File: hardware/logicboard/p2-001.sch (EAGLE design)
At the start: 33 parts, among them IC1 5V, IC2 74LS07N, IC3 4066N, IC4 LTC485N, K1 G5V1, T1 2SC1815, U1 DS18B20

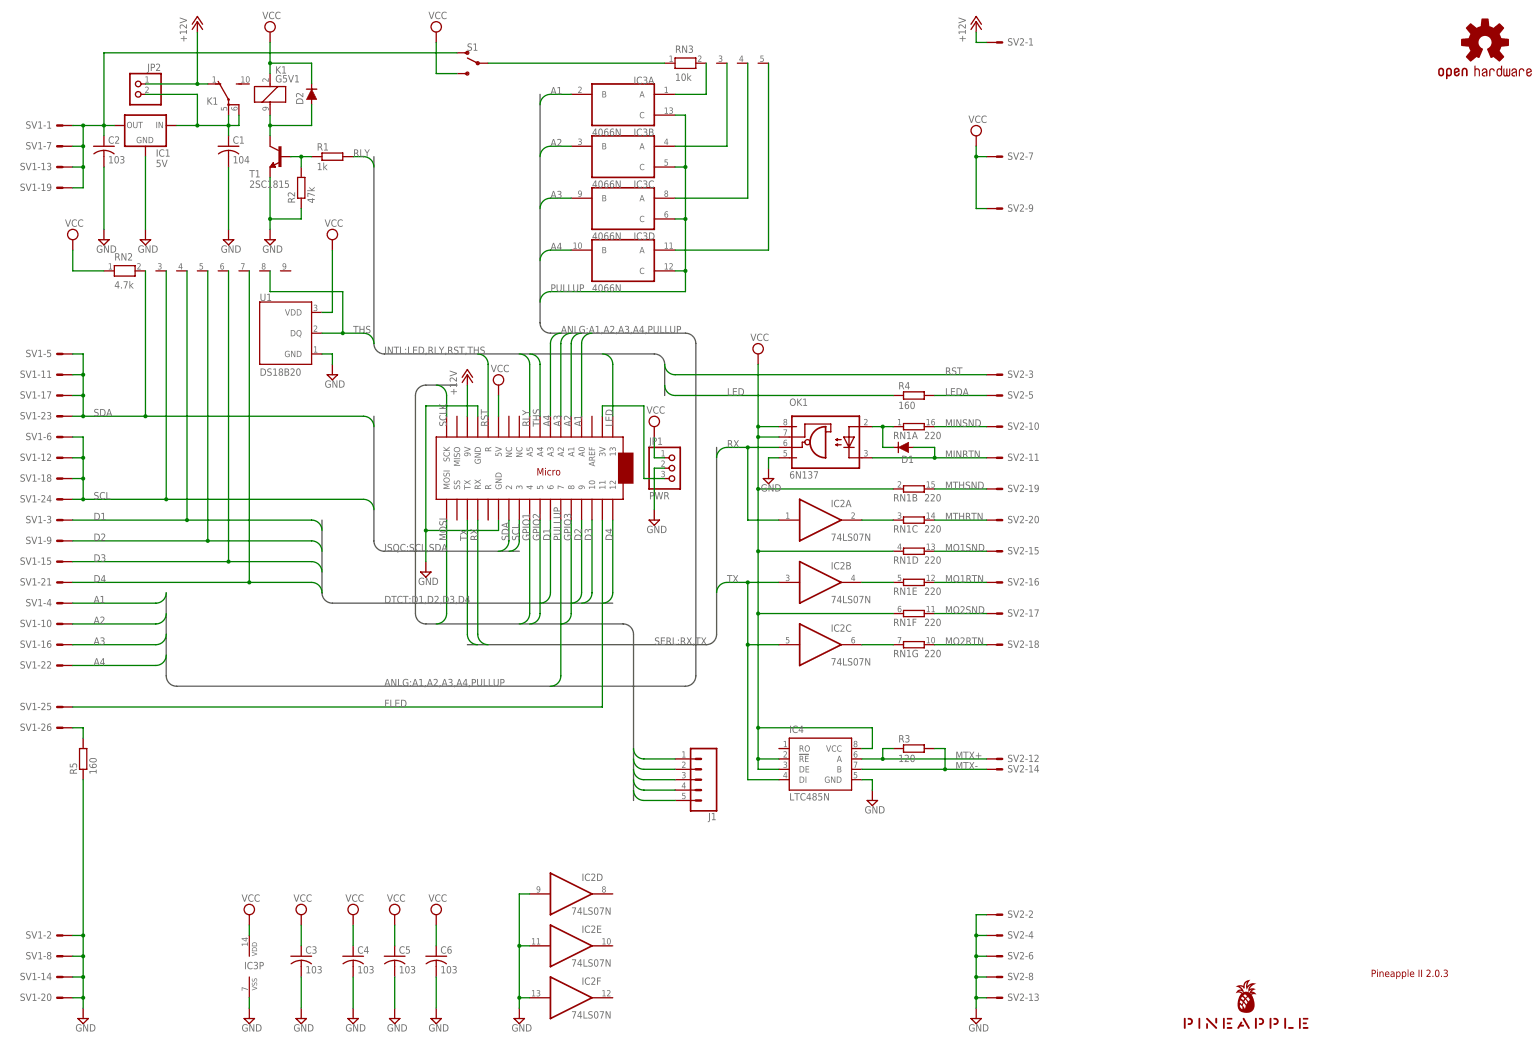
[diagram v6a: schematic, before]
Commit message: Renumbered parts.
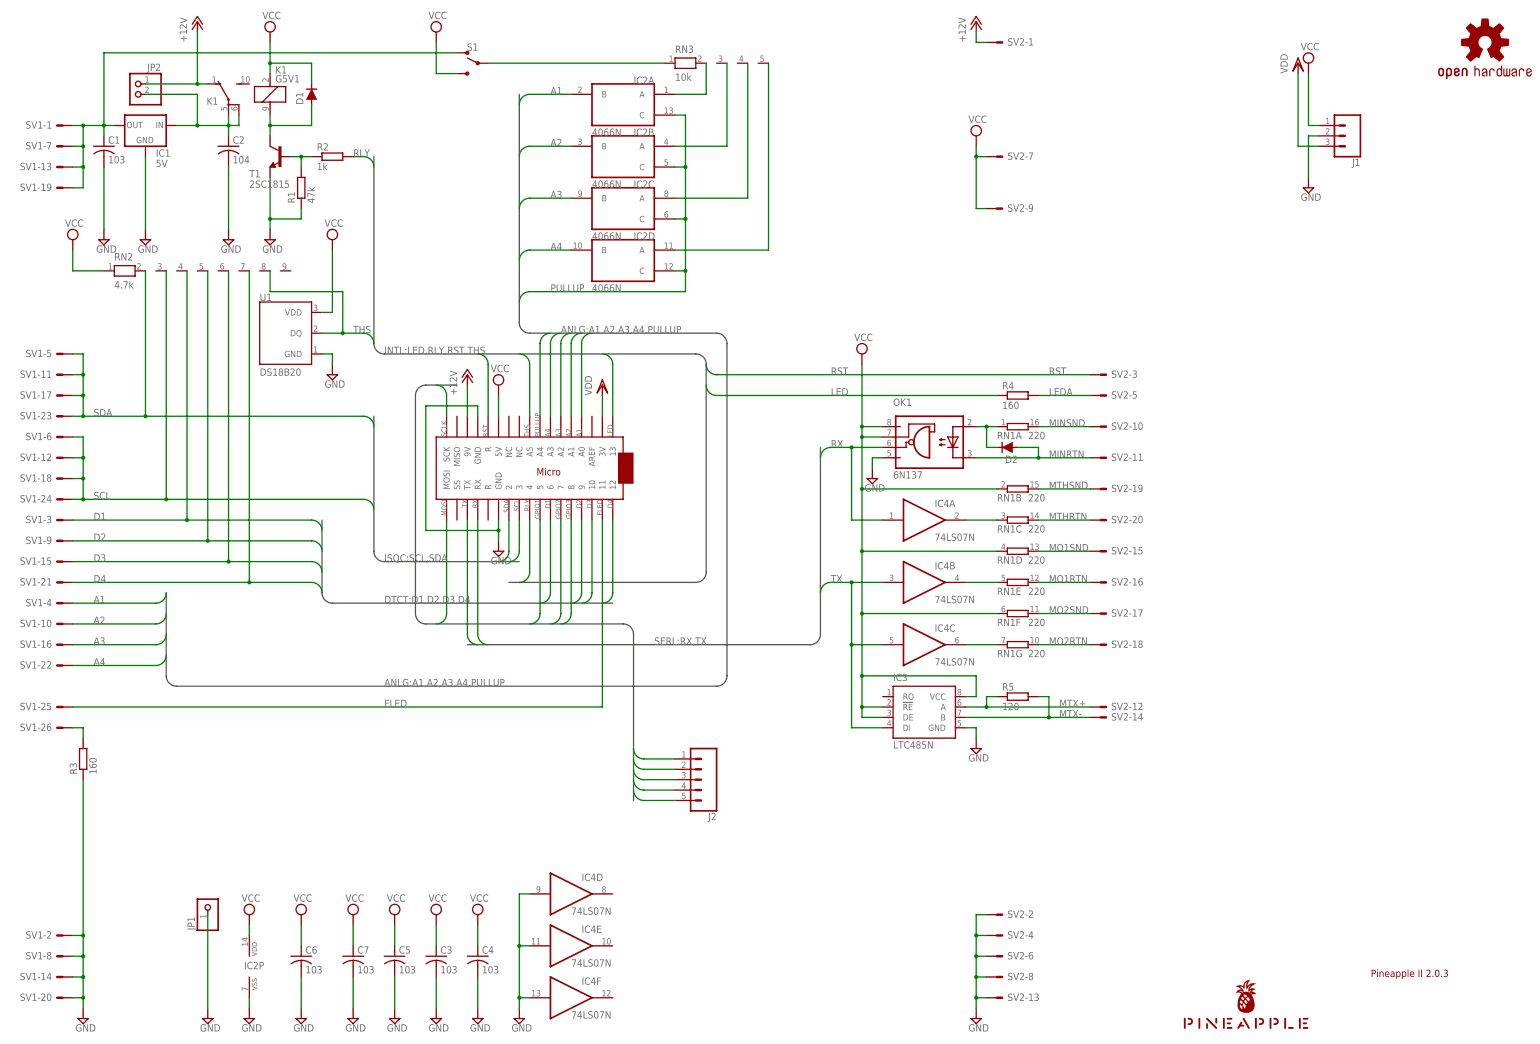
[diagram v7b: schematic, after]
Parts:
- added C7: 103, rcl:C-US025-025X050
- added J2: (no value), SparkFun-Connectors:CONN_05JST
- C1: value 104 -> 103
- C2: value 103 -> 104
- IC2: value 74LS07N -> 4066N; device 74xx-us:74LS07N -> 40xx:4066N
- IC3: value 4066N -> LTC485N; device 40xx:4066N -> linear-technology:LTC485N
- IC4: value LTC485N -> 74LS07N; device linear-technology:LTC485N -> 74xx-us:74LS07N
- J1: device SparkFun-Connectors:CONN_05JST -> SparkFun-Connectors:CONN_03JST-PTH
- JP1: value PWR -> (none); device pinhead:PINHD-1X3 -> pinhead:PINHD-1X1
- R1: value 1k -> 47k
- R2: value 47k -> 1k
- R3: value 120 -> 160
- R5: value 160 -> 120
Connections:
- removed net N$1: R5.2, SV1-26.S
- new net FLEDK: R3.2, SV1-26.S
- net A1: now also IC2A.B; no longer IC3A.B
- net A2: now also IC2B.B; no longer IC3B.B
- net A3: now also IC2C.B; no longer IC3C.B
- net A4: now also IC2D.B; no longer IC3D.B
- net GND: now also C7.2, IC2P.VSS, IC3.GND, IC4D.I, IC4E.I, IC4F.I, J1.2, JP1.1, R1.1, R3.1; no longer IC2D.I, IC2E.I, IC2F.I, IC3P.VSS, IC4.GND, JP1.2, R2.1, R5.1
- net GPIO1: now also J2.3, MC1.5; no longer J1.3, MC1.4
- net GPIO2: now also J2.4, MC1.7; no longer J1.4, MC1.5
- net GPIO3: now also J2.5; no longer J1.5
- net MIDIINSND: now also D2.C; no longer D1.C
- net MIDIOUT2RTN: now also IC4C.O; no longer IC2C.O
- net MIDIOUTRTN: now also IC4B.O; no longer IC2B.O
- net MIDITHRURTN: now also IC4A.O; no longer IC2A.O
- net MINRTN: now also D2.A; no longer D1.A
- net MOSI: now also J2.1; no longer J1.1
- net MTX+: now also IC3.A, R5.1; no longer IC4.A, R3.1
- net MTX-: now also IC3.B, R5.2; no longer IC4.B, R3.2
- net N$3: now also IC2A.A; no longer IC3A.A
- net N$4: now also IC2B.A; no longer IC3B.A
- net N$5: now also IC2C.A; no longer IC3C.A
- net N$6: now also IC2D.A; no longer IC3D.A
- net PULLUP: now also IC2A.C, IC2B.C, IC2C.C, IC2D.C, MC1.A4; no longer IC3A.C, IC3B.C, IC3C.C, IC3D.C, MC1.7
- net RLY: now also MC1.4, R2.2; no longer MC1.A5, R1.2
- net RLYDRV: now also R1.2, R2.1; no longer R1.1, R2.2
- net RLYSNK: now also D1.A; no longer D2.A
- net RX: now also IC4A.I; no longer IC2A.I
- net SCLK: now also J2.2; no longer J1.2
- net THS: now also MC1.A5; no longer MC1.A4
- net TX: now also IC3.DI, IC4B.I, IC4C.I; no longer IC2B.I, IC2C.I, IC4.DI
- net V+12V: now also C2.1; no longer C1.1
- net VCC: now also C7.1, D1.C, IC2P.VDD, IC3.!RE, IC3.DE, IC3.VCC, J1.1; no longer D2.C, IC3P.VDD, IC4.!RE, IC4.DE, IC4.VCC, JP1.1
- net VDD: now also J1.3; no longer JP1.3
- net VOUT: now also C1.1; no longer C2.1
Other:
- moved on the sheet: C1, C2, C3, C4, C6, D1, D2, OK1, R1, R2, R3, R4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

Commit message: Readability.
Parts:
- added JP3: RELAYJUMP, pinhead:PINHD-1X2
- J1: value (none) -> Power
- J2: value (none) -> Display
- JP1: value (none) -> GNDPIN
- JP2: value (none) -> PWRSPL; device pinhead:PINHD-1X2 -> pinhead:PINHD-1X3
- S1: value (none) -> AnalogPullUpSelect
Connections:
- removed net FLEDK: R3.2, SV1-26.S
- removed net V+12V: C2.1, IC1.IN, JP2.2, K12.P, K12.P@1
- removed net VOUT: C1.1, IC1.OUT, S1.O, SV1-1.S, SV1-13.S, SV1-19.S, SV1-7.S
- new net +5V: C1.1, IC1.OUT, JP2.3, S1.O, SV1-1.S, SV1-13.S, SV1-19.S, SV1-7.S
- new net N$2: R3.1, SV1-26.S
- new net VIN: C2.1, IC1.IN, JP2.1, JP3.2, K12.P, K12.P@1
- net +12V: now also JP3.1; no longer JP2.1
- net GND: now also JP2.2, R3.2; no longer R3.1
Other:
- moved on the sheet: C1, C2, C3, C4, C5, C6, C7, D1, D2, IC1, IC2A, IC2B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
